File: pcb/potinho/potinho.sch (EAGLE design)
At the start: 16 parts, among them IC1 MEGA8-AI, IC2 LM1117-5.0, IC3 LM1117-3.3, IC31 HC-SR04, IC4 NRF24L01

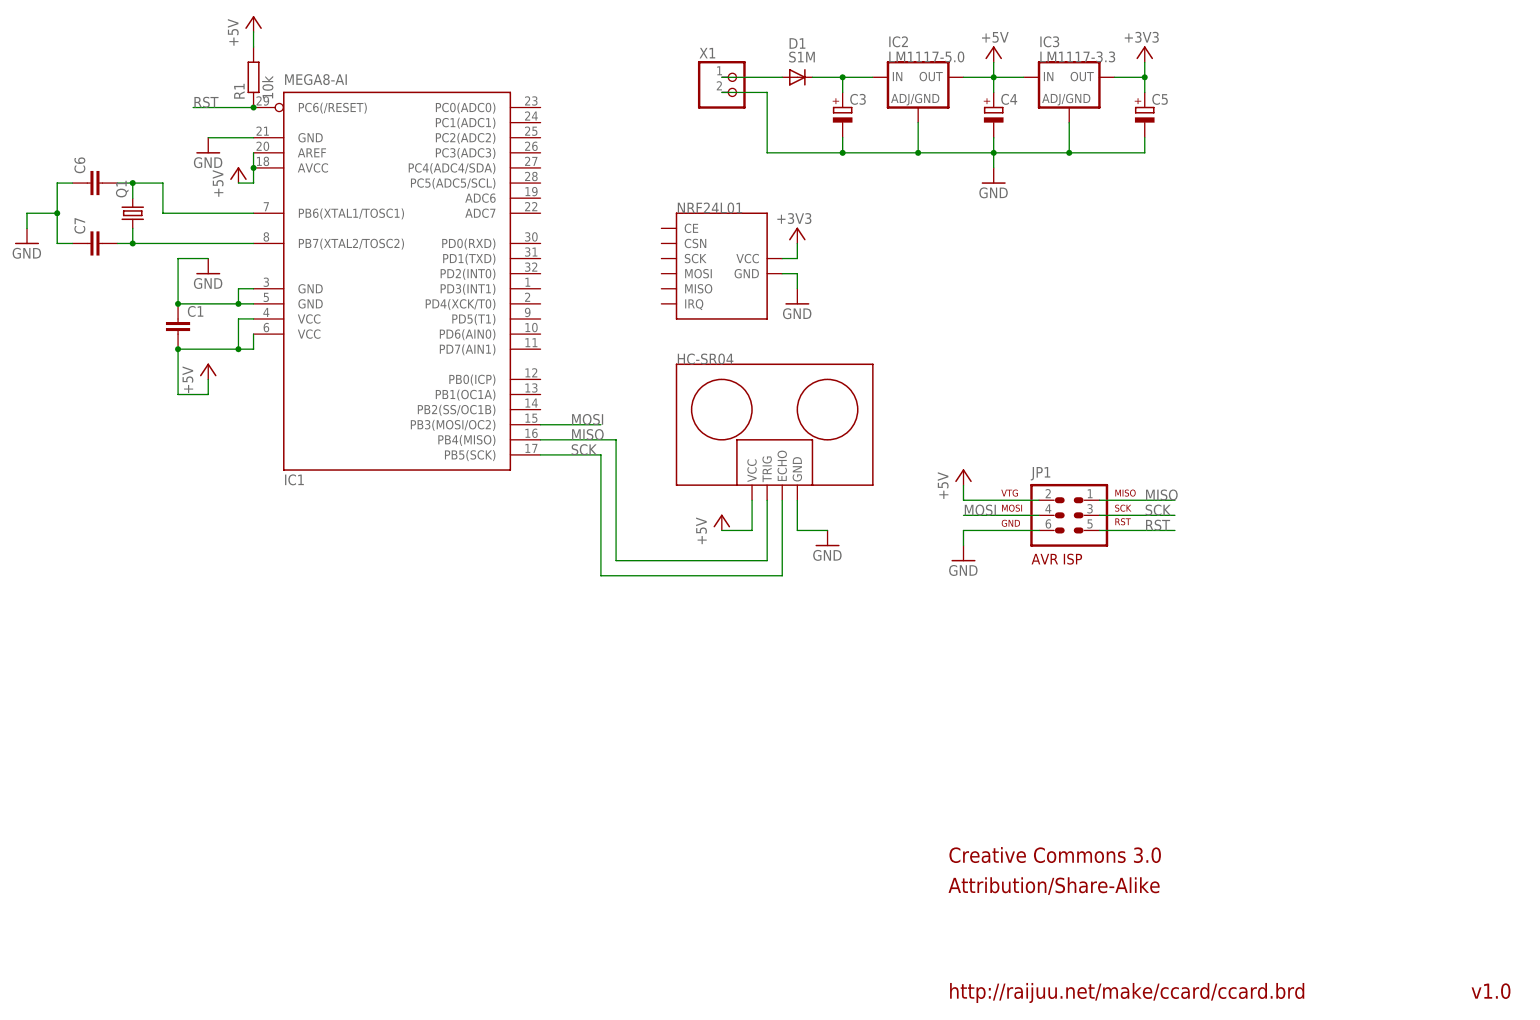
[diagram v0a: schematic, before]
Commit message: 
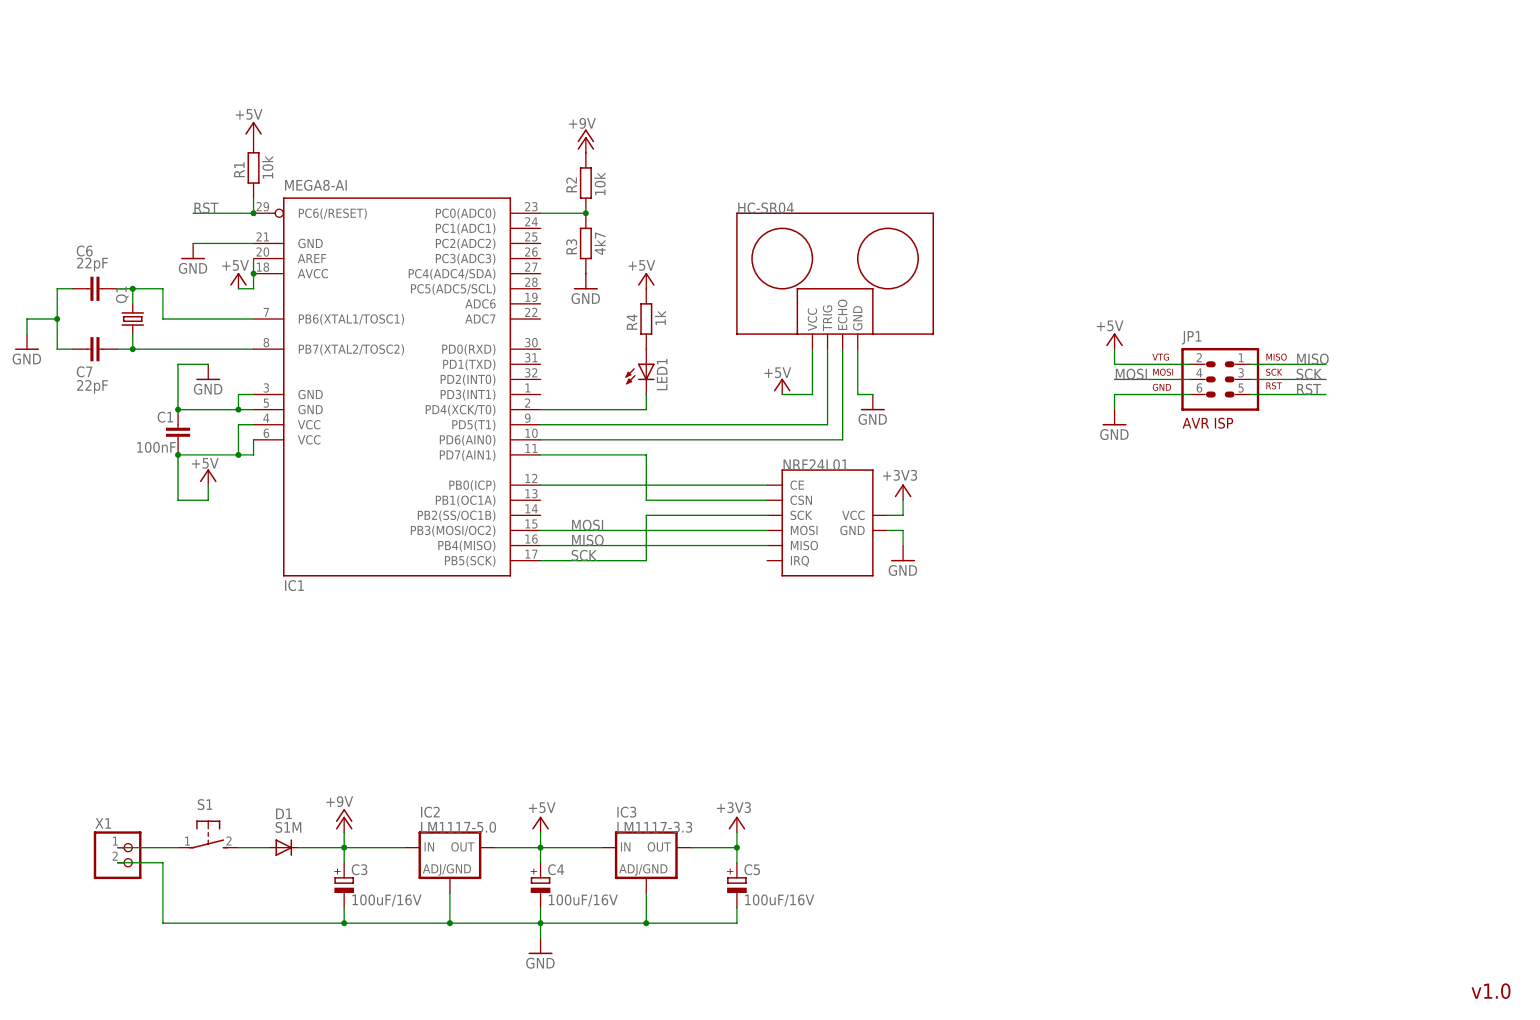
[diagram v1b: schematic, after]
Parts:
- added LED1: (no value), potinho:LED3MM
- added R2: 10k, potinho:R-EU_7
- added R3: 4k7, potinho:R-EU_7
- added R4: 1k, potinho:R-EU_7
- added S1: (no value), potinho:31-XX
- C1: value (none) -> 100nF
- C3, C4, C5: value (none) -> 100uF/16V
- C6, C7: value (none) -> 22pF
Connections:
- new net +12V: C3.+, D1.C, IC2.IN, R2.2
- new net N$10: IC1.PD4(XCK/T0), LED1.C
- new net N$11: LED1.A, R4.1
- new net N$2: IC1.PB0(ICP), IC4.CE
- new net N$4: IC1.PD7(AIN1), IC4.CSN
- new net N$7: IC1.PD5(T1), IC31.TRIG
- new net N$8: IC1.PD6(AIN0), IC31.ECHO
- new net N$9: S1.P, X1.1
- net +5V: now also R4.2
- net GND: now also R3.1
- net MISO: now also IC4.MISO; no longer IC31.TRIG
- net MOSI: now also IC4.MOSI
- net N$1: now also S1.S; no longer X1.1
- net N$3: now also IC1.PC0(ADC0), R2.1, R3.2; no longer C3.+, D1.C, IC2.IN
- net SCK: now also IC4.SCK; no longer IC31.ECHO
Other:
- note removed: "Attribution/Share-Alike"
- note removed: "Creative Commons 3.0"
- note removed: "http://raijuu.net/make/ccard/ccard.brd"
- moved on the sheet: C1, C3, C4, C5, C6, C7, D1, IC1, IC2, IC3, JP1, Q1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
